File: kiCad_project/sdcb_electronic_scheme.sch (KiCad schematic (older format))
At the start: 74 parts, among them CON1 SD_Card, J1 POWER_12V, J10 BUTTON_RIGHT_TURN, J11 DB9, J2 Arduino_Nano_Header, J3 REAL_TIME_CLOCK, J4 LEFT_TURN_GYRO, J5 RIGHT_TURN_GYRO, J6 POWER_12V, J7 MOTOR, J9 BUTTON_LEFT_TURN, Q1 BC817-40, Q2 BC817-40, U1 74HC595, U2 74HC165N, U3 74HC165N

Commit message: Added libs
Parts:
- gave numbers to parts that had none: 1
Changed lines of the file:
@@
 $EndComp
 $Comp
-L +12V #PWR4
+L +12V #PWR01
 U 1 1 55B7FB0B
 P 3550 900
-F 0 "#PWR4" H 3550 750 50  0001 C CNN
+F 0 "#PWR01" H 3550 750 50  0001 C CNN
 F 1 "+12V" H 3550 1040 50  0000 C CNN
 F 2 "" H 3550 900 60  0000 C CNN
@@
 $EndComp
 $Comp
-L GND #PWR5
+L GND #PWR02
 U 1 1 55B7FB2D
 P 3550 2350
-F 0 "#PWR5" H 3550 2100 50  0001 C CNN
+F 0 "#PWR02" H 3550 2100 50  0001 C CNN
 F 1 "GND" H 3550 2200 50  0000 C CNN
 F 2 "" H 3550 2350 60  0000 C CNN
@@
 $EndComp
 $Comp
-L GND #PWR2
+L GND #PWR03
 U 1 1 55B9174E
 P 1950 7500
-F 0 "#PWR2" H 1950 7250 50  0001 C CNN
+F 0 "#PWR03" H 1950 7250 50  0001 C CNN
 F 1 "GND" H 1950 7350 50  0000 C CNN
 F 2 "" H 1950 7500 60  0000 C CNN
@@
 $EndComp
 $Comp
-L +5V #PWR17
+L +5V #PWR04
 U 1 1 55BD5738
 P 6250 3600
-F 0 "#PWR17" H 6250 3450 50  0001 C CNN
+F 0 "#PWR04" H 6250 3450 50  0001 C CNN
 F 1 "+5V" H 6250 3740 50  0000 C CNN
 F 2 "" H 6250 3600 60  0000 C CNN
@@
 $EndComp
 $Comp
-L +5V #PWR23
+L +5V #PWR05
 U 1 1 55BD59FF
 P 7150 4950
-F 0 "#PWR23" H 7150 4800 50  0001 C CNN
+F 0 "#PWR05" H 7150 4800 50  0001 C CNN
 F 1 "+5V" H 7150 5090 50  0000 C CNN
 F 2 "" H 7150 4950 60  0000 C CNN
@@
 $EndComp
 $Comp
-L +3.3V #PWR18
+L +3.3V #PWR06
 U 1 1 55BD7A33
 P 6250 4600
-F 0 "#PWR18" H 6250 4450 50  0001 C CNN
+F 0 "#PWR06" H 6250 4450 50  0001 C CNN
 F 1 "+3.3V" H 6250 4740 50  0000 C CNN
 F 2 "" H 6250 4600 60  0000 C CNN
@@
 $EndComp
 $Comp
-L +12V #PWR16
+L +12V #PWR07
 U 1 1 55BDA058
 P 6250 3300
-F 0 "#PWR16" H 6250 3150 50  0001 C CNN
+F 0 "#PWR07" H 6250 3150 50  0001 C CNN
 F 1 "+12V" H 6250 3440 50  0000 C CNN
 F 2 "" H 6250 3300 60  0000 C CNN
@@
 $EndComp
 $Comp
-L GND #PWR20
+L GND #PWR08
 U 1 1 55BDA311
 P 6550 3400
-F 0 "#PWR20" H 6550 3150 50  0001 C CNN
+F 0 "#PWR08" H 6550 3150 50  0001 C CNN
 F 1 "GND" H 6550 3250 50  0000 C CNN
 F 2 "" H 6550 3400 60  0000 C CNN
@@
 $EndComp
 $Comp
-L GND #PWR11
+L GND #PWR09
 U 1 1 55BDB4FB
 P 4950 3600
-F 0 "#PWR11" H 4950 3350 50  0001 C CNN
+F 0 "#PWR09" H 4950 3350 50  0001 C CNN
 F 1 "GND" H 4950 3450 50  0000 C CNN
 F 2 "" H 4950 3600 60  0000 C CNN
@@
 $EndComp
 $Comp
-L GND #PWR15
+L GND #PWR010
 U 1 1 55BDD4CE
 P 6200 1450
-F 0 "#PWR15" H 6200 1200 50  0001 C CNN
+F 0 "#PWR010" H 6200 1200 50  0001 C CNN
 F 1 "GND" H 6200 1300 50  0000 C CNN
 F 2 "" H 6200 1450 60  0000 C CNN
@@
 $EndComp
 $Comp
-L GND #PWR12
+L GND #PWR011
 U 1 1 55BDD564
 P 5600 950
-F 0 "#PWR12" H 5600 700 50  0001 C CNN
+F 0 "#PWR011" H 5600 700 50  0001 C CNN
 F 1 "GND" H 5600 800 50  0000 C CNN
 F 2 "" H 5600 950 60  0000 C CNN
@@
 $EndComp
 $Comp
-L GND #PWR32
+L GND #PWR012
 U 1 1 55BE259A
 P 10150 3350
-F 0 "#PWR32" H 10150 3100 50  0001 C CNN
+F 0 "#PWR012" H 10150 3100 50  0001 C CNN
 F 1 "GND" H 10150 3200 50  0000 C CNN
 F 2 "" H 10150 3350 60  0000 C CNN
@@
 $EndComp
 $Comp
-L GND #PWR24
+L GND #PWR013
 U 1 1 55BE8F6B
 P 7300 5000
-F 0 "#PWR24" H 7300 4750 50  0001 C CNN
+F 0 "#PWR013" H 7300 4750 50  0001 C CNN
 F 1 "GND" H 7300 4850 50  0000 C CNN
 F 2 "" H 7300 5000 60  0000 C CNN
@@
 $EndComp
 $Comp
-L GND #PWR28
+L GND #PWR014
 U 1 1 55BEBCC6
 P 7700 6300
-F 0 "#PWR28" H 7700 6050 50  0001 C CNN
+F 0 "#PWR014" H 7700 6050 50  0001 C CNN
 F 1 "GND" H 7700 6150 50  0000 C CNN
 F 2 "" H 7700 6300 60  0000 C CNN
@@
 $EndComp
 $Comp
-L +5V #PWR25
+L +5V #PWR015
 U 1 1 55BF5B34
 P 7450 3650
-F 0 "#PWR25" H 7450 3500 50  0001 C CNN
+F 0 "#PWR015" H 7450 3500 50  0001 C CNN
 F 1 "+5V" H 7450 3790 50  0000 C CNN
 F 2 "" H 7450 3650 60  0000 C CNN
@@
 $EndComp
 $Comp
-L +5V #PWR26
+L +5V #PWR016
 U 1 1 55BF5BA0
 P 7450 4350
-F 0 "#PWR26" H 7450 4200 50  0001 C CNN
+F 0 "#PWR016" H 7450 4200 50  0001 C CNN
 F 1 "+5V" H 7450 4490 50  0000 C CNN
 F 2 "" H 7450 4350 60  0000 C CNN
@@
 $EndComp
 $Comp
-L GND #PWR27
+L GND #PWR017
 U 1 1 55BF6554
 P 7600 4850
-F 0 "#PWR27" H 7600 4600 50  0001 C CNN
+F 0 "#PWR017" H 7600 4600 50  0001 C CNN
 F 1 "GND" H 7600 4700 50  0000 C CNN
 F 2 "" H 7600 4850 60  0000 C CNN
@@
 $EndComp
 $Comp
-L GND #PWR29
+L GND #PWR018
 U 1 1 55BA7F17
 P 7850 2100
-F 0 "#PWR29" H 7850 1850 50  0001 C CNN
+F 0 "#PWR018" H 7850 1850 50  0001 C CNN
 F 1 "GND" H 7850 1950 50  0000 C CNN
 F 2 "" H 7850 2100 60  0000 C CNN
@@
 $EndComp
 $Comp
-L GND #PWR31
+L GND #PWR019
 U 1 1 55BB31C6
 P 9750 800
-F 0 "#PWR31" H 9750 550 50  0001 C CNN
+F 0 "#PWR019" H 9750 550 50  0001 C CNN
 F 1 "GND" H 9750 650 50  0000 C CNN
 F 2 "" H 9750 800 60  0000 C CNN
@@
 $EndComp
 $Comp
-L GND #PWR22
+L GND #PWR020
 U 1 1 55BB6D26
 P 7050 1850
-F 0 "#PWR22" H 7050 1600 50  0001 C CNN
+F 0 "#PWR020" H 7050 1600 50  0001 C CNN
 F 1 "GND" H 7050 1700 50  0000 C CNN
 F 2 "" H 7050 1850 60  0000 C CNN
@@
 $EndComp
 $Comp
-L VCC #PWR19
+L VCC #PWR021
 U 1 1 55BBD6FF
 P 6400 3600
-F 0 "#PWR19" H 6400 3450 50  0001 C CNN
+F 0 "#PWR021" H 6400 3450 50  0001 C CNN
 F 1 "VCC" H 6400 3750 50  0000 C CNN
 F 2 "" H 6400 3600 60  0000 C CNN
@@
 $EndComp
 $Comp
-L GND #PWR8
+L GND #PWR022
 U 1 1 55BC1999
 P 4750 3250
-F 0 "#PWR8" H 4750 3000 50  0001 C CNN
+F 0 "#PWR022" H 4750 3000 50  0001 C CNN
 F 1 "GND" H 4750 3100 50  0000 C CNN
 F 2 "" H 4750 3250 60  0000 C CNN
@@
 $EndComp
 $Comp
-L GND #PWR1
+L GND #PWR023
 U 1 1 55BC538B
 P 1700 3900
-F 0 "#PWR1" H 1700 3650 50  0001 C CNN
+F 0 "#PWR023" H 1700 3650 50  0001 C CNN
 F 1 "GND" H 1700 3750 50  0000 C CNN
 F 2 "" H 1700 3900 60  0000 C CNN
@@
 $EndComp
 $Comp
-L VCC #PWR13
+L VCC #PWR024
 U 1 1 55C11BF7
 P 6050 5400
-F 0 "#PWR13" H 6050 5250 50  0001 C CNN
+F 0 "#PWR024" H 6050 5250 50  0001 C CNN
 F 1 "VCC" H 6050 5550 50  0000 C CNN
 F 2 "" H 6050 5400 60  0000 C CNN
@@
 $EndComp
 $Comp
-L GND #PWR9
+L GND #PWR025
 U 1 1 55C11DBD
 P 4850 6250
-F 0 "#PWR9" H 4850 6000 50  0001 C CNN
+F 0 "#PWR025" H 4850 6000 50  0001 C CNN
 F 1 "GND" H 4850 6100 50  0000 C CNN
 F 2 "" H 4850 6250 60  0000 C CNN
@@
 $EndComp
 $Comp
-L GND #PWR10
+L GND #PWR026
 U 1 1 55C11F82
 P 4850 7400
-F 0 "#PWR10" H 4850 7150 50  0001 C CNN
+F 0 "#PWR026" H 4850 7150 50  0001 C CNN
 F 1 "GND" H 4850 7250 50  0000 C CNN
 F 2 "" H 4850 7400 60  0000 C CNN
@@
 gal čia beeperį dėti?\n
 $Comp
-L +3.3V #PWR3
+L +3.3V #PWR027
 U 1 1 55C26656
 P 2100 6350
-F 0 "#PWR3" H 2100 6200 50  0001 C CNN
+F 0 "#PWR027" H 2100 6200 50  0001 C CNN
 F 1 "+3.3V" H 2100 6490 50  0000 C CNN
 F 2 "" H 2100 6350 60  0000 C CNN
@@
 $EndComp
 $Comp
-L VCC #PWR14
+L VCC #PWR028
 U 1 1 55C2DAEE
 P 6050 6550
-F 0 "#PWR14" H 6050 6400 50  0001 C CNN
+F 0 "#PWR028" H 6050 6400 50  0001 C CNN
 F 1 "VCC" H 6050 6700 50  0000 C CNN
 F 2 "" H 6050 6550 60  0000 C CNN
@@
 $EndComp
 $Comp
-L GND #PWR21
+L GND #PWR029
 U 1 1 55C35CBB
 P 8500 6400
-F 0 "#PWR21" H 8500 6150 50  0001 C CNN
+F 0 "#PWR029" H 8500 6150 50  0001 C CNN
 F 1 "GND" H 8500 6250 50  0000 C CNN
 F 2 "" H 8500 6400 60  0000 C CNN
@@
 Connection ~ 6600 6600
 $Comp
-L GND #PWR6
+L GND #PWR030
 U 1 1 55C3ED4C
 P 4200 3150
-F 0 "#PWR6" H 4200 2900 50  0001 C CNN
+F 0 "#PWR030" H 4200 2900 50  0001 C CNN
 F 1 "GND" H 4200 3000 50  0000 C CNN
 F 2 "" H 4200 3150 60  0000 C CNN
@@
 $EndComp
 $Comp
-L VCC #PWR7
+L VCC #PWR031
 U 1 1 55C3EE35
 P 4200 3450
-F 0 "#PWR7" H 4200 3300 50  0001 C CNN
+F 0 "#PWR031" H 4200 3300 50  0001 C CNN
 F 1 "VCC" H 4200 3600 50  0000 C CNN
 F 2 "" H 4200 3450 60  0000 C CNN
@@
 kaip čia šitoj vietoj?
 $Comp
-L VCC #PWR?
+L VCC #PWR032
 U 1 1 55C19181
 P 6900 6600
-F 0 "#PWR?" H 6900 6450 50  0001 C CNN
+F 0 "#PWR032" H 6900 6450 50  0001 C CNN
 F 1 "VCC" H 6900 6750 50  0000 C CNN
 F 2 "" H 6900 6600 60  0000 C CNN
@@
 $EndComp
 $Comp
-L DB15 J?
+L DB15 J8
 U 1 1 55C1D46B
 P 10750 4450
-F 0 "J?" H 10770 5300 70  0000 C CNN
+F 0 "J8" H 10770 5300 70  0000 C CNN
 F 1 "DB15" H 10700 3600 70  0000 C CNN
 F 2 "" H 10750 4450 60  0000 C CNN
@@
 	9400 3350 8800 3350
 $Comp
-L GND #PWR?
+L GND #PWR033
 U 1 1 55C28586
 P 8800 3350
-F 0 "#PWR?" H 8800 3100 50  0001 C CNN
+F 0 "#PWR033" H 8800 3100 50  0001 C CNN
 F 1 "GND" H 8800 3200 50  0000 C CNN
 F 2 "" H 8800 3350 60  0000 C CNN

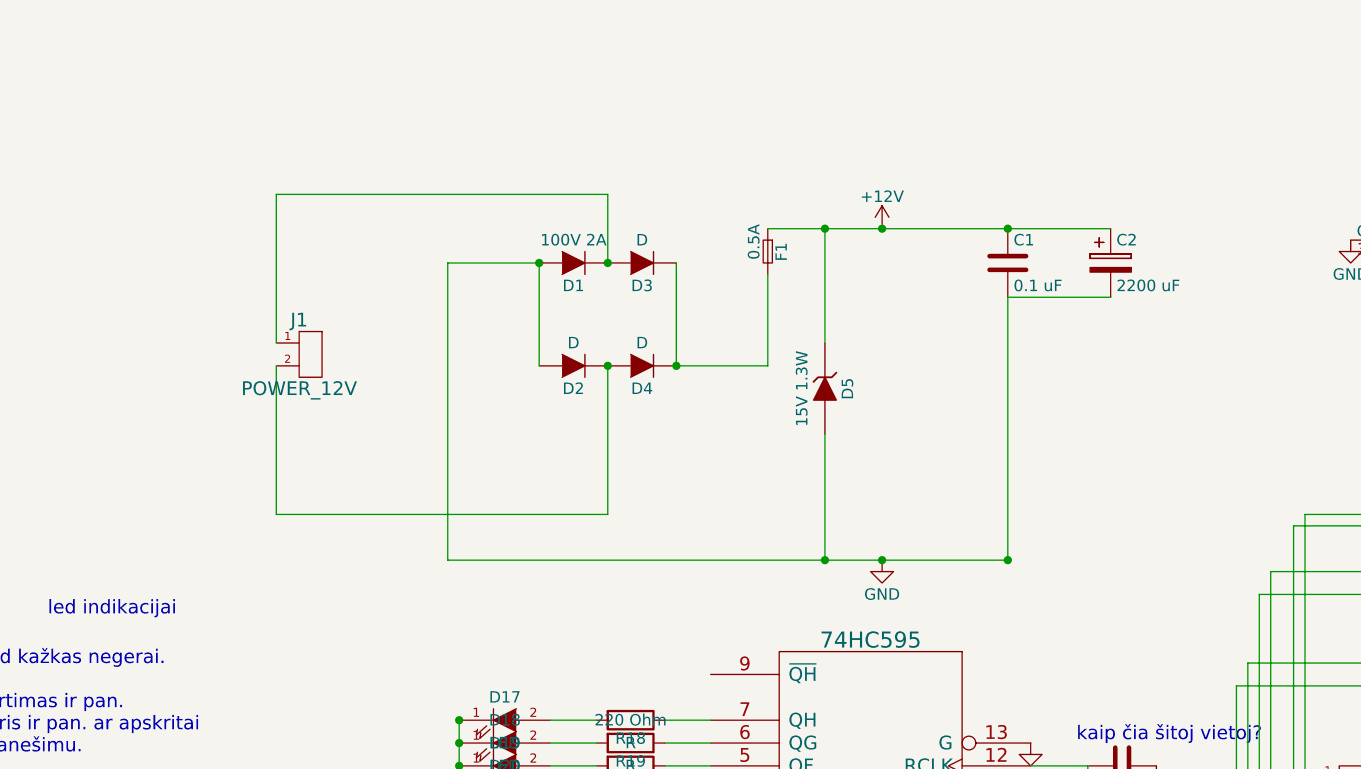
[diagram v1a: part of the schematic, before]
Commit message: refactoring power rectification and smoothing circuit
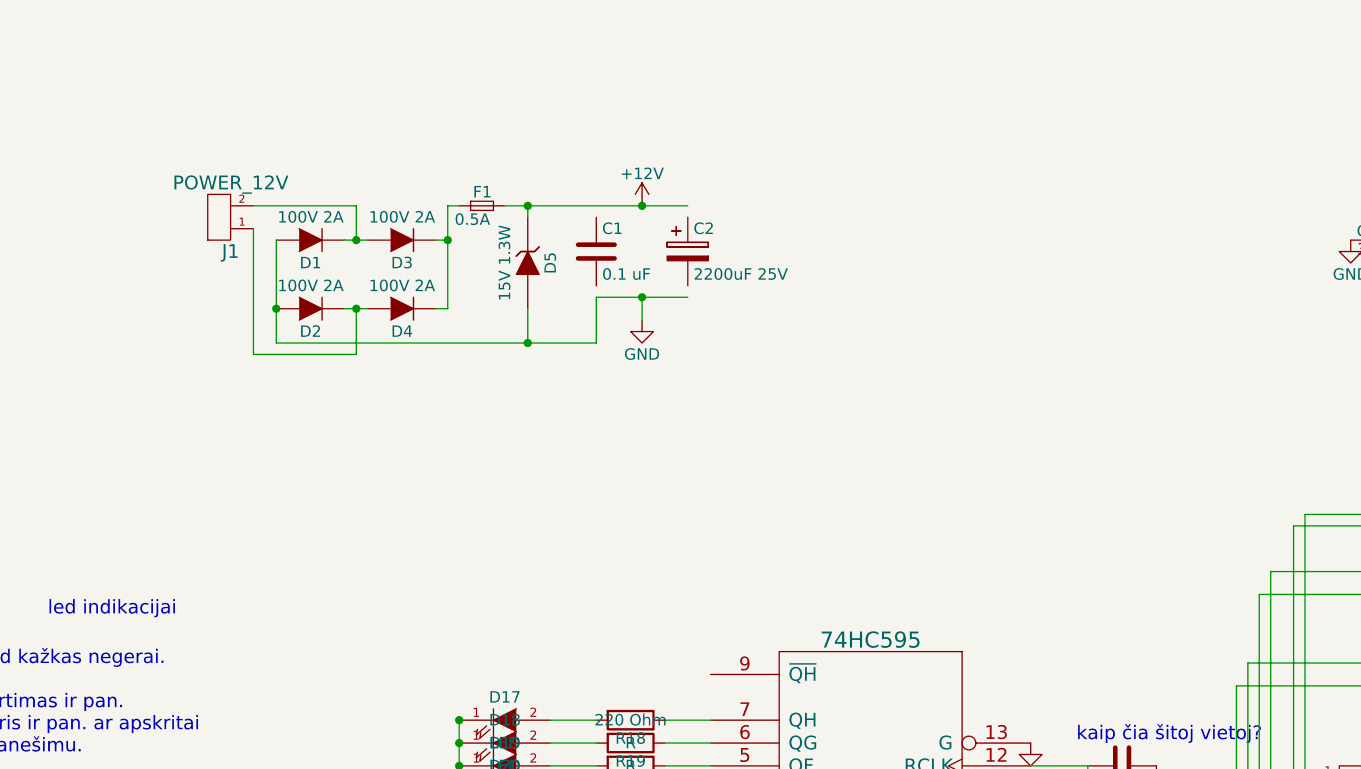
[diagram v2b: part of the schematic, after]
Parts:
- C2: value 2200 uF -> 2200uF 25V
- D2, D3, D4: value D -> 100V 2A
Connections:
- wire segments 206 -> 207
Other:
- moved on the sheet: C1, C2, D1, D2, D3, D4, D5, F1, J1
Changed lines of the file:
@@
 LIBS:contrib
 LIBS:valves
-LIBS:arduino
-LIBS:w_connectors
-LIBS:relays_2
-LIBS:nais_tq2sa_smd_relay
-LIBS:switch_dpdt
-LIBS:switch_spdt
 LIBS:relays
 LIBS:sdcb_electronic_scheme-cache
-EELAYER 25 0
+EELAYER 27 0
 EELAYER END
 $Descr A4 11693 8268
@@
 Sheet 1 1
 Title ""
-Date ""
+Date "4 aug 2015"
 Rev ""
 Comp ""
@@
 L HEADER_2 J1
 U 1 1 55B7F512
-P 1000 1450
-F 0 "J1" H 1000 1600 60  0000 C CNN
-F 1 "POWER_12V" H 1000 1300 60  0000 C CNN
-F 2 "Pin_Headers:Pin_Header_Straight_2x01" H 1000 1450 60  0001 C CNN
-F 3 "" H 1000 1450 60  0000 C CNN
-	1    1000 1450
-	1    0    0    -1
+P 700 850
+F 0 "J1" H 700 1000 60  0000 C CNN
+F 1 "POWER_12V" H 700 700 60  0000 C CNN
+F 2 "Pin_Headers:Pin_Header_Straight_2x01" H 700 850 60  0001 C CNN
+F 3 "" H 700 850 60  0000 C CNN
+	1    700  850
+	-1   0    0    1
 $EndComp
 $Comp
 L C C1
 U 1 1 55B7F855
-P 4100 1050
-F 0 "C1" H 4125 1150 50  0000 L CNN
-F 1 "0.1 uF" H 4125 950 50  0000 L CNN
-F 2 "Capacitors_ThroughHole:C_Disc_D6_P5" H 4138 900 30  0001 C CNN
-F 3 "" H 4100 1050 60  0000 C CNN
-	1    4100 1050
+P 2300 1000
+F 0 "C1" H 2325 1100 50  0000 L CNN
+F 1 "0.1 uF" H 2325 900 50  0000 L CNN
+F 2 "Capacitors_ThroughHole:C_Disc_D6_P5" H 2338 850 30  0001 C CNN
+F 3 "" H 2300 1000 60  0000 C CNN
+	1    2300 1000
 	1    0    0    -1
 $EndComp
@@
 L CP C2
 U 1 1 55B7F95A
-P 4550 1050
-F 0 "C2" H 4575 1150 50  0000 L CNN
-F 1 "2200 uF" H 4575 950 50  0000 L CNN
-F 2 "Capacitors_Elko_ThroughHole:Elko_vert_25x14mm_RM5_CopperClear" H 4588 900 30  0001 C CNN
-F 3 "" H 4550 1050 60  0000 C CNN
-	1    4550 1050
+P 2700 1000
+F 0 "C2" H 2725 1100 50  0000 L CNN
+F 1 "2200uF 25V" H 2725 900 50  0000 L CNN
+F 2 "Capacitors_Elko_ThroughHole:Elko_vert_25x14mm_RM5_CopperClear" H 2738 850 30  0001 C CNN
+F 3 "" H 2700 1000 60  0000 C CNN
+	1    2700 1000
 	1    0    0    -1
 $EndComp
@@
 L +12V #PWR01
 U 1 1 55B7FB0B
-P 3550 900
-F 0 "#PWR01" H 3550 750 50  0001 C CNN
-F 1 "+12V" H 3550 1040 50  0000 C CNN
-F 2 "" H 3550 900 60  0000 C CNN
-F 3 "" H 3550 900 60  0000 C CNN
-	1    3550 900
+P 2500 800
+F 0 "#PWR01" H 2500 650 50  0001 C CNN
+F 1 "+12V" H 2500 940 50  0000 C CNN
+F 2 "" H 2500 800 60  0000 C CNN
+F 3 "" H 2500 800 60  0000 C CNN
+	1    2500 800
 	1    0    0    -1
 $EndComp
@@
 L GND #PWR02
 U 1 1 55B7FB2D
-P 3550 2350
-F 0 "#PWR02" H 3550 2100 50  0001 C CNN
-F 1 "GND" H 3550 2200 50  0000 C CNN
-F 2 "" H 3550 2350 60  0000 C CNN
-F 3 "" H 3550 2350 60  0000 C CNN
-	1    3550 2350
+P 2500 1300
+F 0 "#PWR02" H 2500 1050 50  0001 C CNN
+F 1 "GND" H 2500 1150 50  0000 C CNN
+F 2 "" H 2500 1300 60  0000 C CNN
+F 3 "" H 2500 1300 60  0000 C CNN
+	1    2500 1300
 	1    0    0    -1
 $EndComp
@@
 L ZENER D5
 U 1 1 55B808ED
-P 3300 1600
-F 0 "D5" H 3300 1700 50  0000 C CNN
-F 1 "15V 1.3W" H 3300 1500 50  0000 C CNN
-F 2 "Discret:D3" H 3300 1600 60  0001 C CNN
-F 3 "" H 3300 1600 60  0000 C CNN
-	1    3300 1600
+P 2000 1050
+F 0 "D5" H 2000 1150 50  0000 C CNN
+F 1 "15V 1.3W" H 2000 950 50  0000 C CNN
+F 2 "Discret:D3" H 2000 1050 60  0001 C CNN
+F 3 "" H 2000 1050 60  0000 C CNN
+	1    2000 1050
 	0    1    1    0
 $EndComp
@@
 L F_Small F1
 U 1 1 55B80C11
-P 3050 1000
-F 0 "F1" H 3010 1060 50  0000 L CNN
-F 1 "0.5A" H 2930 940 50  0000 L CNN
-F 2 "fuse:fuse_05A_slot" H 3050 1000 60  0001 C CNN
-F 3 "" H 3050 1000 60  0000 C CNN
-	1    3050 1000
-	0    1    1    0
+P 1800 800
+F 0 "F1" H 1760 860 50  0000 L CNN
+F 1 "0.5A" H 1680 740 50  0000 L CNN
+F 2 "fuse:fuse_05A_slot" H 1800 800 60  0001 C CNN
+F 3 "" H 1800 800 60  0000 C CNN
+	1    1800 800
+	1    0    0    -1
 $EndComp
 $Comp
 L D D3
 U 1 1 55B80F33
-P 2500 1050
-F 0 "D3" H 2500 1150 50  0000 C CNN
-F 1 "D" H 2500 950 50  0000 C CNN
-F 2 "Diodes_ThroughHole:Diode_DO-201AD_Horizontal_RM15" H 2500 1050 60  0001 C CNN
-F 3 "" H 2500 1050 60  0000 C CNN
-	1    2500 1050
+P 1450 950
+F 0 "D3" H 1450 1050 50  0000 C CNN
+F 1 "100V 2A" H 1450 850 50  0000 C CNN
+F 2 "Diodes_ThroughHole:Diode_DO-201AD_Horizontal_RM15" H 1450 950 60  0001 C CNN
+F 3 "" H 1450 950 60  0000 C CNN
+	1    1450 950
 	-1   0    0    1
 $EndComp
@@
 L D D4
 U 1 1 55B8108A
-P 2500 1500
-F 0 "D4" H 2500 1600 50  0000 C CNN
-F 1 "D" H 2500 1400 50  0000 C CNN
-F 2 "Diodes_ThroughHole:Diode_DO-201AD_Horizontal_RM15" H 2500 1500 60  0001 C CNN
-F 3 "" H 2500 1500 60  0000 C CNN
-	1    2500 1500
+P 1450 1250
+F 0 "D4" H 1450 1350 50  0000 C CNN
+F 1 "100V 2A" H 1450 1150 50  0000 C CNN
+F 2 "Diodes_ThroughHole:Diode_DO-201AD_Horizontal_RM15" H 1450 1250 60  0001 C CNN
+F 3 "" H 1450 1250 60  0000 C CNN
+	1    1450 1250
 	-1   0    0    1
 $EndComp
@@
 L D D2
 U 1 1 55B8110B
-P 2200 1500
-F 0 "D2" H 2200 1600 50  0000 C CNN
-F 1 "D" H 2200 1400 50  0000 C CNN
-F 2 "Diodes_ThroughHole:Diode_DO-201AD_Horizontal_RM15" H 2200 1500 60  0001 C CNN
-F 3 "" H 2200 1500 60  0000 C CNN
-	1    2200 1500
+P 1050 1250
+F 0 "D2" H 1050 1350 50  0000 C CNN
+F 1 "100V 2A" H 1050 1150 50  0000 C CNN
+F 2 "Diodes_ThroughHole:Diode_DO-201AD_Horizontal_RM15" H 1050 1250 60  0001 C CNN
+F 3 "" H 1050 1250 60  0000 C CNN
+	1    1050 1250
 	-1   0    0    1
 $EndComp
@@
 L D D1
 U 1 1 55B81168
-P 2200 1050
-F 0 "D1" H 2200 1150 50  0000 C CNN
-F 1 "100V 2A" H 2200 950 50  0000 C CNN
-F 2 "Diodes_ThroughHole:Diode_DO-201AD_Horizontal_RM15" H 2200 1050 60  0001 C CNN
-F 3 "" H 2200 1050 60  0000 C CNN
-	1    2200 1050
+P 1050 950
+F 0 "D1" H 1050 1050 50  0000 C CNN
+F 1 "100V 2A" H 1050 850 50  0000 C CNN
+F 2 "Diodes_ThroughHole:Diode_DO-201AD_Horizontal_RM15" H 1050 950 60  0001 C CNN
+F 3 "" H 1050 950 60  0000 C CNN
+	1    1050 950
 	-1   0    0    1
 $EndComp
@@
 $EndComp
 Wire Wire Line
-	900  1500 900  2150
-Wire Wire Line
-	900  2150 2350 2150
-Wire Wire Line
-	900  1400 900  750
-Wire Wire Line
-	900  750  2350 750
-Wire Wire Line
-	3050 900  4550 900
-Connection ~ 4100 900
-Wire Wire Line
-	4100 2350 1650 2350
-Wire Wire Line
-	1650 2350 1650 1050
-Wire Wire Line
-	3300 1400 3300 900
-Connection ~ 3300 900
-Wire Wire Line
-	3050 1100 3050 1500
-Wire Wire Line
-	1650 1050 2050 1050
-Wire Wire Line
-	2050 1050 2050 1500
-Wire Wire Line
-	2350 750  2350 1050
-Wire Wire Line
-	2650 1050 2650 1500
-Wire Wire Line
-	2650 1500 3050 1500
-Wire Wire Line
-	2350 2150 2350 1500
-Connection ~ 2050 1050
-Connection ~ 2350 1500
-Connection ~ 2650 1500
-Connection ~ 2350 1050
-Wire Wire Line
 	950  6800 950  7000
 Wire Wire Line
@@
 Wire Wire Line
 	1450 6500 1450 4400
-Connection ~ 4100 2350
 Wire Wire Line
 	5350 3400 5450 3400
@@
 	6150 3400 6550 3400
 Wire Wire Line
-	3300 1800 3300 2350
-Connection ~ 3300 2350
-Wire Wire Line
 	5450 3600 4950 3600
 Wire Wire Line
@@
 Wire Wire Line
 	6400 1350 6400 1250
-Wire Wire Line
-	4550 1200 4100 1200
-Wire Wire Line
-	4100 1200 4100 2350
 Connection ~ 9400 3350
 Connection ~ 9200 3350
@@
 Wire Wire Line
 	1700 3050 1700 3900
-Connection ~ 3550 900
-Connection ~ 3550 2350
 Wire Wire Line
 	9750 700  9450 700
@@
 	1    0    0    -1
 $EndComp
+Wire Wire Line
+	1200 950  1300 950
+Wire Wire Line
+	1250 950  1250 800
+Connection ~ 1250 950
+Wire Wire Line
+	1300 1250 1200 1250
+Wire Wire Line
+	1250 1250 1250 1450
+Wire Wire Line
+	800  1450 800  900
+Connection ~ 1250 1250
+Wire Wire Line
+	900  950  900  1400
+Wire Wire Line
+	1250 800  800  800
+Wire Wire Line
+	1250 1450 800  1450
+Wire Wire Line
+	900  1400 2300 1400
+Connection ~ 900  1250
+Wire Wire Line
+	1900 800  2700 800
+Wire Wire Line
+	2000 800  2000 850
+Wire Wire Line
+	2000 1400 2000 1250
+Wire Wire Line
+	2500 1300 2500 1200
+Wire Wire Line
+	2300 1200 2700 1200
+Connection ~ 2500 1200
+Connection ~ 2000 800
+Wire Wire Line
+	2300 1400 2300 1200
+Connection ~ 2000 1400
+Connection ~ 2500 800
+Wire Wire Line
+	1650 1250 1600 1250
+Wire Wire Line
+	1650 800  1650 1250
+Wire Wire Line
+	1650 950  1600 950
+Connection ~ 1650 950
+Wire Wire Line
+	1650 800  1700 800
 $EndSCHEMATC

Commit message: Schematics updated
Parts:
- removed D10, D12, D13, D14, D15, D8: 5.1V 1.3W, Discret:D3, symbol ZENER
- removed D17: LED, LEDs:LED-3MM, symbol LED
- removed D6, D7: D_Schottky, Diodes_ThroughHole:Diode_DO-41_SOD81_Horizontal_RM10, symbol D_Schottky
- removed J3: REAL_TIME_CLOCK, Pin_Headers:Pin_Header_Straight_1x05, symbol HEADER_5
- removed Q1, Q2: BC817-40, trans:TO-220_Bipolar-BCE_Vertical_LargePads, symbol BC817-40
- removed R11, R12, R16: 100 Ohm, Resistors_ThroughHole:Resistor_Horizontal_RM10mm, symbol R
- removed R13, R14, R15: R, Resistors_ThroughHole:Resistor_Horizontal_RM10mm, symbol R
- removed R17: 10k, symbol R
- removed R18: 220 Ohm, Resistors_ThroughHole:Resistor_Horizontal_RM10mm, symbol R
- removed R26: R, symbol R
- removed R7, R8: 1k, Resistors_ThroughHole:Resistor_Horizontal_RM10mm, symbol R
- removed RL1, RL2: FINDER-36.11.4001, sun_hold:sun_hold_scb1m1240, symbol FINDER-36.11.4001
- removed U2, U3: 74HC165N, symbol 74HC165N
- added D? (x21): D_Schottky, Diodes_ThroughHole:Diode_DO-41_SOD81_Horizontal_RM10, symbol D_Schottky
- added D?: 5.1V 1.3W, Discret:D3, symbol ZENER
- added J?: REAL_TIME_CLOCK, Pin_Headers:Pin_Header_Straight_1x05, symbol HEADER_5
- added J?: HEADER_2, symbol HEADER_2
- added J?: 30V MOTOR, Pin_Headers:Pin_Header_Straight_2x01, symbol HEADER_2
- added J?: 220V, symbol HEADER_2
- added Q? (x3): BC817-40, SOT-23, symbol BC817-40
- added R? (x6): 1k, symbol R
- added R? (x2): 10k, Resistors_ThroughHole:Resistor_Horizontal_RM10mm, symbol R
- added RL? (x3): FINDER-36.11.4001, sun_hold:sun_hold_scb1m1240, symbol FINDER-36.11.4001
- added U? (x3): 74HC595, symbol 74HC595
- added U? (x3): OPTO-TRANSISTOR-4, symbol OPTO-TRANSISTOR-4
- added X?: Buzzer, symbol Buzzer
- J10: value BUTTON_RIGHT_TURN -> B_RIGHT_T
- J9: value BUTTON_LEFT_TURN -> B_LEFT_T
- R19: value R -> 220Ohm
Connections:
- wire segments 207 -> 269
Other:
- note added: "30V variklio rėlė?"
- note added: "???\n"
- note removed: "BUTONAI DIDIEJI??"
- note removed: "diodai patikrai?"
- note removed: "gal čia beeperį dėti?\n"
- note removed: "kaip čia šitoj vietoj?"
- note removed: "nežinau footprintų \nir neaišku, kaip jungsiu."
- note removed: "optronai? bendra žemė?"
- moved on the sheet: C3, CON1, Current1, D11, D18, D19, D20, D21, D22, D23, D24, D9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
